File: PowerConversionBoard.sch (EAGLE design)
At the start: 32 parts, among them Q1 MOSFET_PCH-NDS8434, U3 AZ1117EH-3.3TRG1

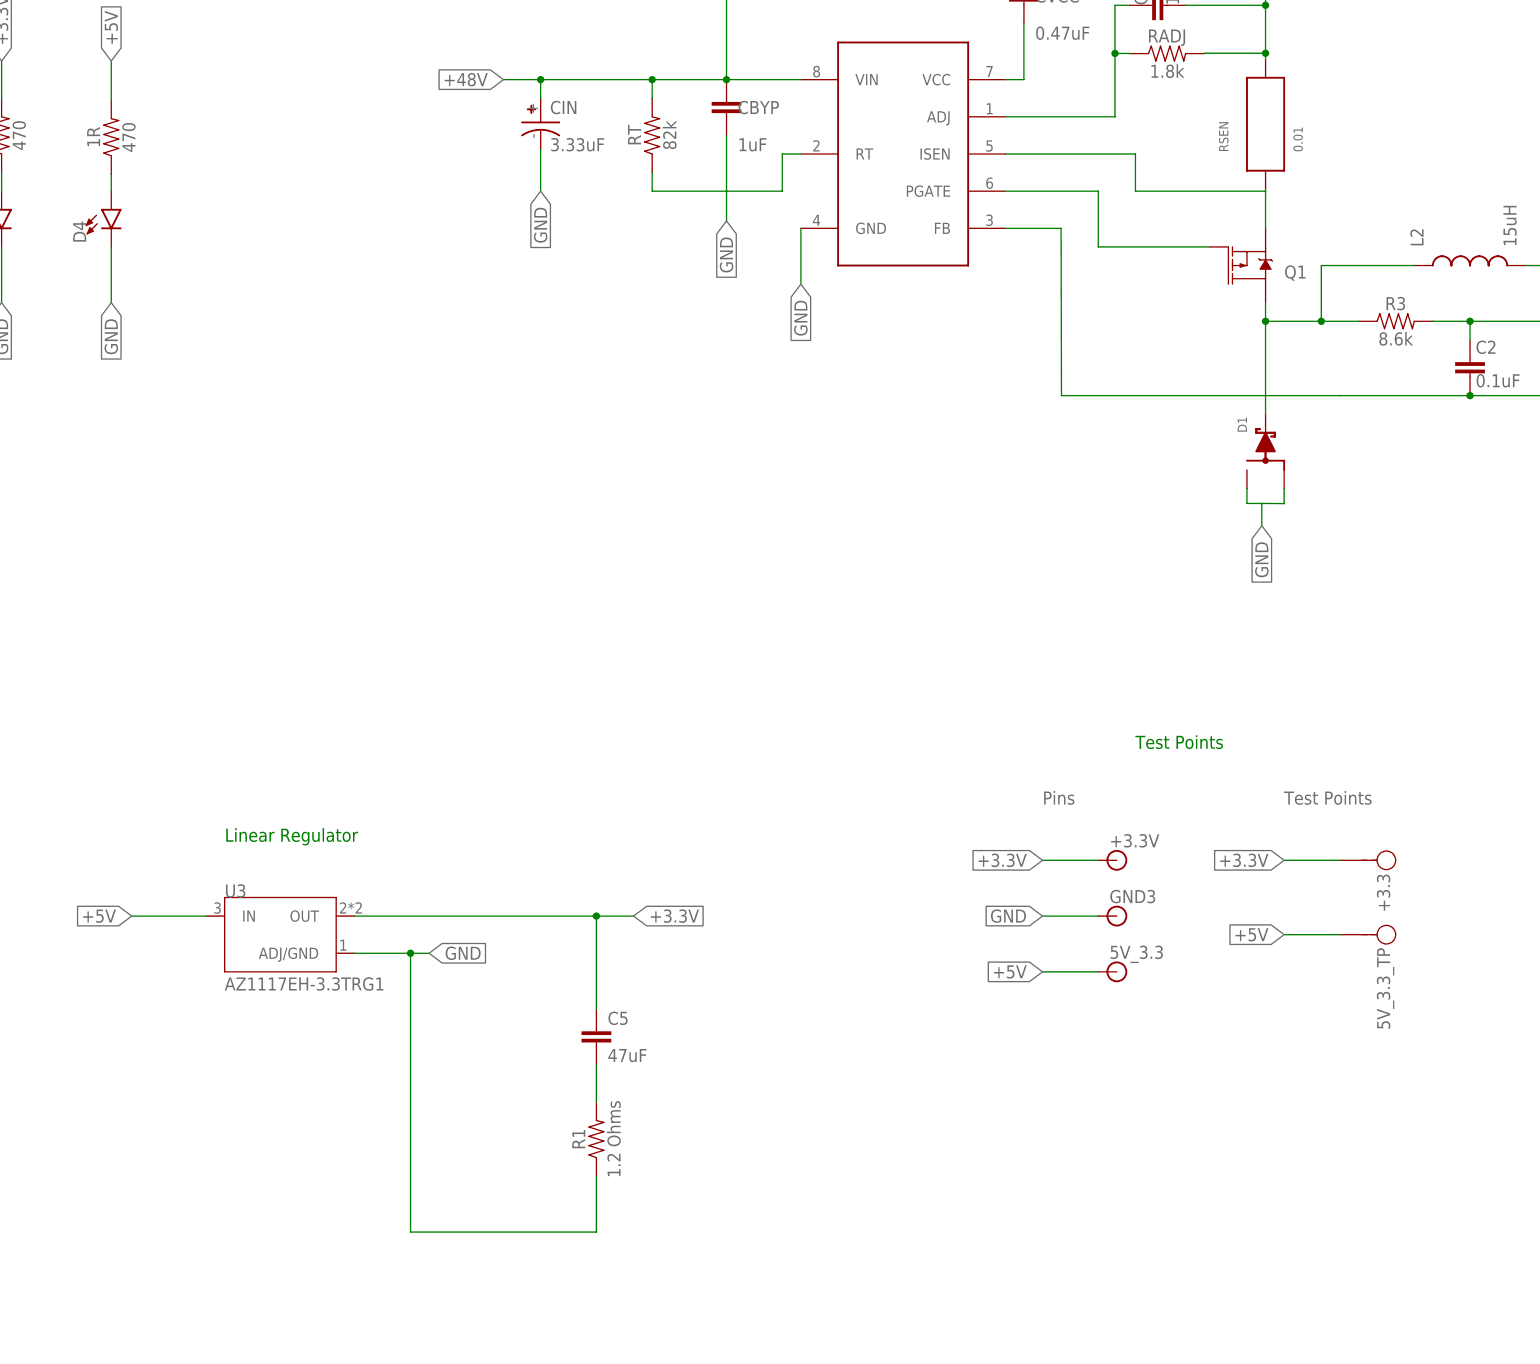
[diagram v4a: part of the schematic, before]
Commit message: Pretty much finished the layput of the board, but a few minor changes still need to be made; awaiting dimensions of potential cutoffs
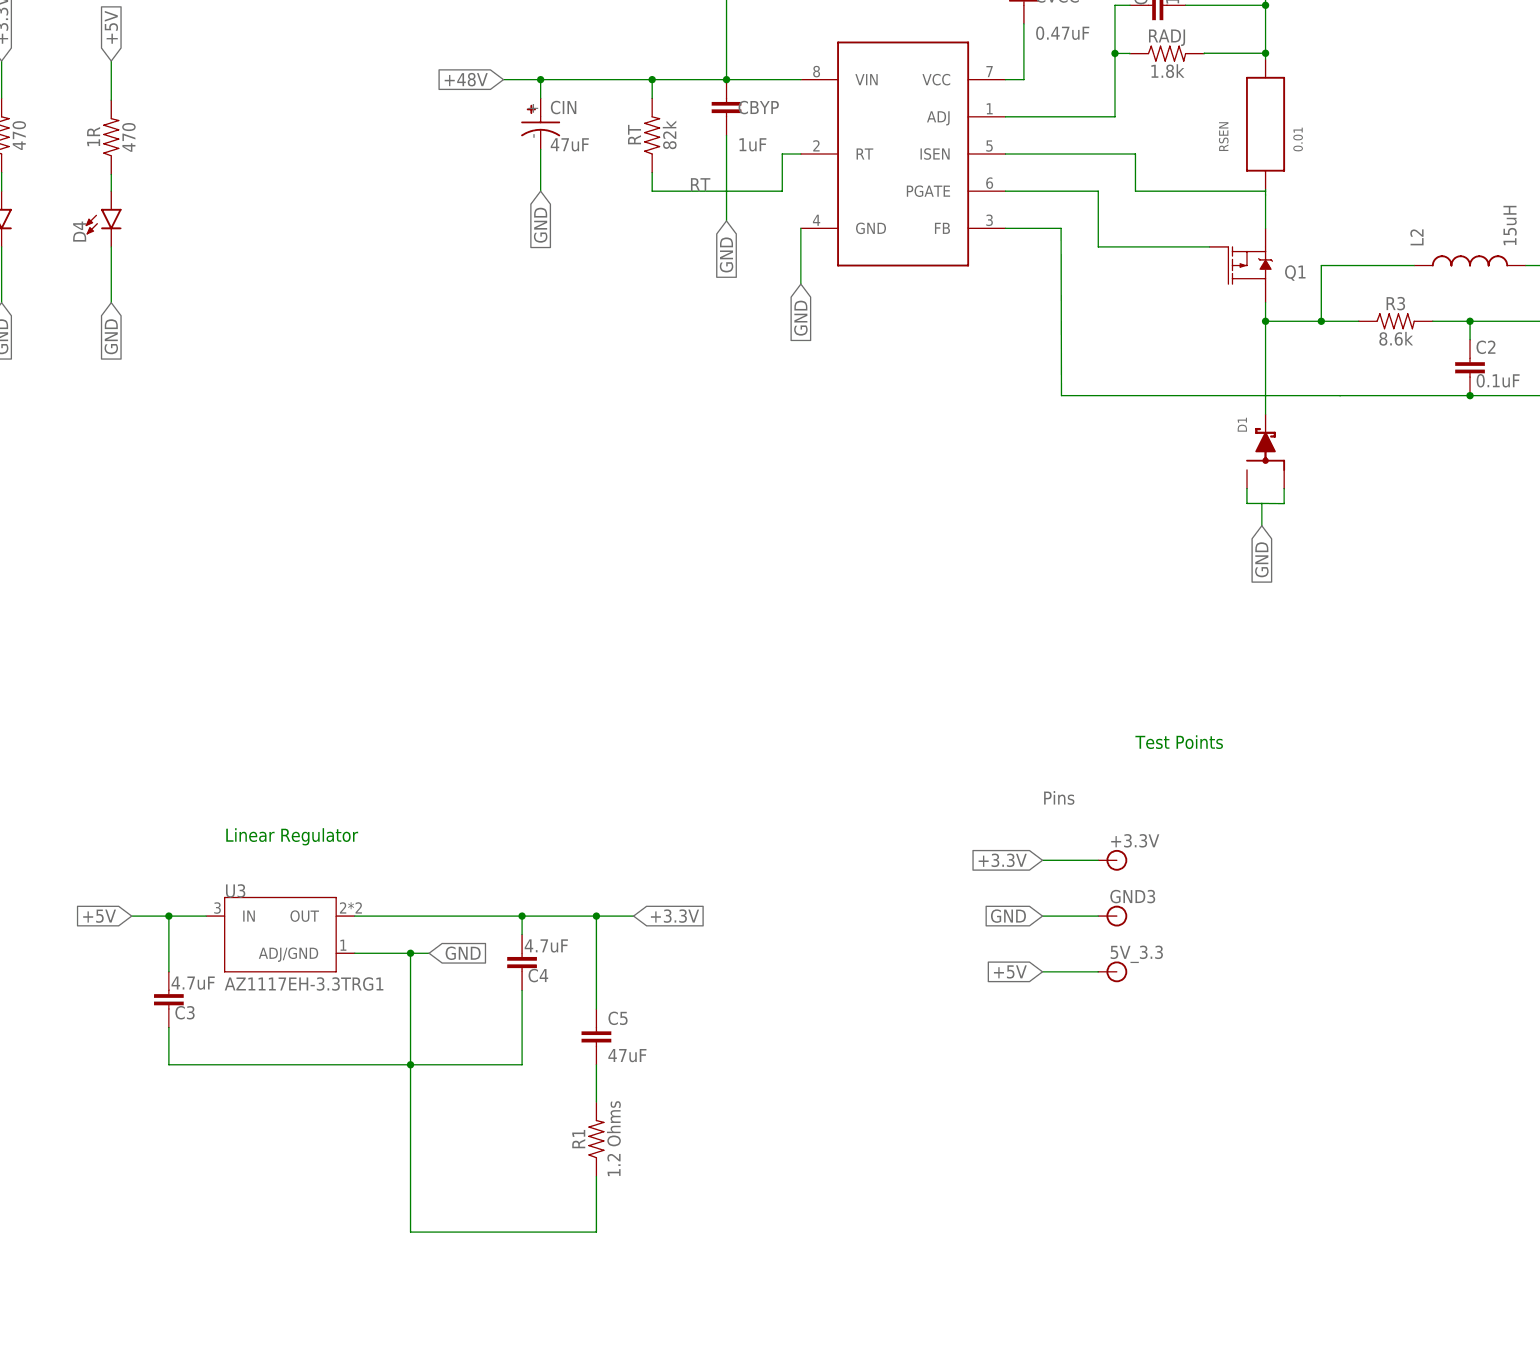
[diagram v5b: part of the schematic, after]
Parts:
- removed +3.3, 5V_3.3_TP: TP, TP:TP
- added C3, C4: 4.7uF, SparkFun-Capacitors:12PF-0603-50V-5%
- CIN: value 3.33uF -> 47uF
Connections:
- new net RT: RT.1, U$1.RT
- net +3.3V: now also C4.1; no longer +3.3.P$1
- net +48V: no longer RT.1, U$1.RT
- net +5V: now also C3.1; no longer 5V_3.3_TP.P$1
- net GND: now also C3.2, C4.2
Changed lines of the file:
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@@
 <part name="D3" library="SparkFun-LED" library_urn="urn:adsk.eagle:library:529" deviceset="LED" device="0603" package3d_urn="urn:adsk.eagle:package:39354/1"/>
 <part name="D4" library="SparkFun-LED" library_urn="urn:adsk.eagle:library:529" deviceset="LED" device="0603" package3d_urn="urn:adsk.eagle:package:39354/1"/>
-<part name="+3.3" library="TP" deviceset="TP" device=""/>
-<part name="5V_3.3_TP" library="TP" deviceset="TP" device=""/>
 <part name="U3" library="Linear Regulator - AZ1117EH-3.3TRG1" deviceset="AZ1117EH-3.3TRG1" device=""/>
 <part name="U$1" library="Buck_Controller" deviceset="LM5085" device=""/>
@@
 <part name="RT" library="SparkFun-Resistors" library_urn="urn:adsk.eagle:library:532" deviceset="82OHM" device="-0603-1/10W-1%" package3d_urn="urn:adsk.eagle:package:39650/1" value="82k"/>
 <part name="C5" library="SparkFun-Capacitors" library_urn="urn:adsk.eagle:library:510" deviceset="0.1UF" device="-0603-25V-5%" package3d_urn="urn:adsk.eagle:package:37414/1" value="47uF"/>
-<part name="CIN" library="brick-capacitor-UCM1H331MNL1GS" deviceset="UCM1H331MNL1GS" device="" package3d_urn="urn:adsk.eagle:package:24202090/2" value="3.33uF"/>
+<part name="CIN" library="brick-capacitor-UCM1H331MNL1GS" deviceset="UCM1H331MNL1GS" device="" package3d_urn="urn:adsk.eagle:package:24202090/2" value="47uF"/>
 <part name="R1" library="SparkFun-Resistors" library_urn="urn:adsk.eagle:library:532" deviceset="1.6KOHM" device="-0603-1/10W-1%" package3d_urn="urn:adsk.eagle:package:39650/1" value="1.2 Ohms"/>
 <part name="COUT" library="PowerComponents" deviceset="C-TANTALUM(10UF_150UF)" device="" value="100uF"/>
@@
 <part name="U$3" library="Dist_Convert_Connector" deviceset="CON2DIST" device=""/>
 <part name="L2" library="Inductor_15uH - hcma1305" deviceset="HCMA1305" device="" package3d_urn="urn:adsk.eagle:package:24201702/2" value="15uH"/>
+<part name="C3" library="SparkFun-Capacitors" library_urn="urn:adsk.eagle:library:510" deviceset="12PF" device="-0603-50V-5%" package3d_urn="urn:adsk.eagle:package:37414/1" value="4.7uF"/>
+<part name="C4" library="SparkFun-Capacitors" library_urn="urn:adsk.eagle:library:510" deviceset="12PF" device="-0603-50V-5%" package3d_urn="urn:adsk.eagle:package:37414/1" value="4.7uF"/>
 </parts>
 <sheets>
 <sheet>
 <plain>
-<text x="246.38" y="106.68" size="1.778" layer="95">Test Points</text>
 <text x="213.36" y="106.68" size="1.778" layer="95">Pins</text>
 <text x="101.6" y="101.6" size="1.778" layer="91">Linear Regulator</text>
@@
 <attribute name="VALUE" x="88.011" y="183.388" size="1.778" layer="96" font="vector" rot="R90" align="top-left"/>
 </instance>
-<instance part="+3.3" gate="G$1" x="256.54" y="99.06" smashed="yes" rot="R270">
-<attribute name="NAME" x="259.08" y="97.282" size="1.778" layer="95" rot="R270"/>
-</instance>
-<instance part="5V_3.3_TP" gate="G$1" x="256.54" y="88.9" smashed="yes" rot="R270">
-<attribute name="NAME" x="259.08" y="87.122" size="1.778" layer="95" rot="R270"/>
-</instance>
 <instance part="U3" gate="G$1" x="109.22" y="88.9" smashed="yes">
 <attribute name="NAME" x="101.59058125" y="93.98628125" size="1.7802" layer="95"/>
@@
 <attribute name="NAME" x="265.43" y="182.88" size="1.778" layer="95" rot="R90"/>
 <attribute name="VALUE" x="278.13" y="182.88" size="1.778" layer="96" rot="R90"/>
+</instance>
+<instance part="C3" gate="G$1" x="93.98" y="78.74" smashed="yes">
+<attribute name="NAME" x="94.742" y="77.343" size="1.778" layer="95"/>
+<attribute name="VALUE" x="94.234" y="81.407" size="1.778" layer="96"/>
+</instance>
+<instance part="C4" gate="G$1" x="142.24" y="83.82" smashed="yes">
+<attribute name="NAME" x="143.002" y="82.423" size="1.778" layer="95"/>
+<attribute name="VALUE" x="142.494" y="86.487" size="1.778" layer="96"/>
 </instance>
 </instances>
@@
 <label x="129.54" y="86.36" size="1.778" layer="95" xref="yes"/>
 <wire x1="127" y1="86.36" x2="129.54" y2="86.36" width="0.1524" layer="91"/>
-<wire x1="127" y1="48.26" x2="127" y2="86.36" width="0.1524" layer="91"/>
+<wire x1="127" y1="48.26" x2="127" y2="71.12" width="0.1524" layer="91"/>
 <junction x="127" y="86.36"/>
 <pinref part="R1" gate="G$1" pin="1"/>
+<wire x1="127" y1="71.12" x2="127" y2="86.36" width="0.1524" layer="91"/>
 <wire x1="152.4" y1="55.88" x2="152.4" y2="48.26" width="0.1524" layer="91"/>
 <wire x1="127" y1="48.26" x2="152.4" y2="48.26" width="0.1524" layer="91"/>
+<pinref part="C3" gate="G$1" pin="2"/>
+<wire x1="93.98" y1="76.2" x2="93.98" y2="71.12" width="0.1524" layer="91"/>
+<wire x1="93.98" y1="71.12" x2="127" y2="71.12" width="0.1524" layer="91"/>
+<junction x="127" y="71.12"/>
+<pinref part="C4" gate="G$1" pin="2"/>
+<wire x1="142.24" y1="81.28" x2="142.24" y2="71.12" width="0.1524" layer="91"/>
+<wire x1="142.24" y1="71.12" x2="127" y2="71.12" width="0.1524" layer="91"/>
 </segment>
 <segment>
@@
 </segment>
 <segment>
-<wire x1="254" y1="99.06" x2="246.38" y2="99.06" width="0.1524" layer="91"/>
-<label x="246.38" y="99.06" size="1.778" layer="95" rot="R180" xref="yes"/>
-<pinref part="+3.3" gate="G$1" pin="P$1"/>
-</segment>
-<segment>
 <pinref part="U3" gate="G$1" pin="OUT"/>
-<wire x1="119.38" y1="91.44" x2="152.4" y2="91.44" width="0.1524" layer="91"/>
+<wire x1="119.38" y1="91.44" x2="142.24" y2="91.44" width="0.1524" layer="91"/>
 <label x="157.48" y="91.44" size="1.778" layer="95" xref="yes"/>
 <pinref part="C5" gate="G$1" pin="1"/>
+<wire x1="142.24" y1="91.44" x2="152.4" y2="91.44" width="0.1524" layer="91"/>
 <wire x1="152.4" y1="91.44" x2="157.48" y2="91.44" width="0.1524" layer="91"/>
 <wire x1="152.4" y1="78.74" x2="152.4" y2="91.44" width="0.1524" layer="91"/>
 <junction x="152.4" y="91.44"/>
+<pinref part="C4" gate="G$1" pin="1"/>
+<wire x1="142.24" y1="88.9" x2="142.24" y2="91.44" width="0.1524" layer="91"/>
+<junction x="142.24" y="91.44"/>
 </segment>
 <segment>
@@
 </segment>
 <segment>
-<label x="246.38" y="88.9" size="1.778" layer="95" rot="R180" xref="yes"/>
-<wire x1="254" y1="88.9" x2="246.38" y2="88.9" width="0.1524" layer="91"/>
-<pinref part="5V_3.3_TP" gate="G$1" pin="P$1"/>
-</segment>
-<segment>
 <pinref part="U3" gate="G$1" pin="IN"/>
-<wire x1="99.06" y1="91.44" x2="88.9" y2="91.44" width="0.1524" layer="91"/>
+<wire x1="99.06" y1="91.44" x2="93.98" y2="91.44" width="0.1524" layer="91"/>
 <label x="88.9" y="91.44" size="1.778" layer="95" rot="R180" xref="yes"/>
+<pinref part="C3" gate="G$1" pin="1"/>
+<wire x1="93.98" y1="91.44" x2="88.9" y2="91.44" width="0.1524" layer="91"/>
+<wire x1="93.98" y1="83.82" x2="93.98" y2="91.44" width="0.1524" layer="91"/>
+<junction x="93.98" y="91.44"/>
 </segment>
 <segment>
@@
 </segment>
 <segment>
-<pinref part="U$1" gate="G$1" pin="RT"/>
-<wire x1="180.34" y1="195.58" x2="177.8" y2="195.58" width="0.1524" layer="91"/>
-<wire x1="177.8" y1="195.58" x2="177.8" y2="190.5" width="0.1524" layer="91"/>
-<wire x1="177.8" y1="190.5" x2="160.02" y2="190.5" width="0.1524" layer="91"/>
-<wire x1="160.02" y1="190.5" x2="160.02" y2="193.04" width="0.1524" layer="91"/>
-<pinref part="RT" gate="G$1" pin="1"/>
-</segment>
-<segment>
 <pinref part="U$3" gate="G$1" pin="VIN+"/>
 <wire x1="157.861" y1="-108.585" x2="144.78" y2="-108.585" width="0.1524" layer="91"/>
@@
 </segment>
 </net>
+<net name="RT" class="0">
+<segment>
+<pinref part="U$1" gate="G$1" pin="RT"/>
+<wire x1="180.34" y1="195.58" x2="177.8" y2="195.58" width="0.1524" layer="91"/>
+<wire x1="177.8" y1="195.58" x2="177.8" y2="190.5" width="0.1524" layer="91"/>
+<wire x1="177.8" y1="190.5" x2="160.02" y2="190.5" width="0.1524" layer="91"/>
+<wire x1="160.02" y1="190.5" x2="160.02" y2="193.04" width="0.1524" layer="91"/>
+<pinref part="RT" gate="G$1" pin="1"/>
+<label x="165.1" y="190.5" size="1.778" layer="95"/>
+</segment>
+</net>
